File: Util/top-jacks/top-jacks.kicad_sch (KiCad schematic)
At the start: 6 parts, among them J1 Screw_Terminal_01x02, J4 Barrel_Jack_Switch, J5 Screw_Terminal_01x06, J6 Screw_Terminal_01x02

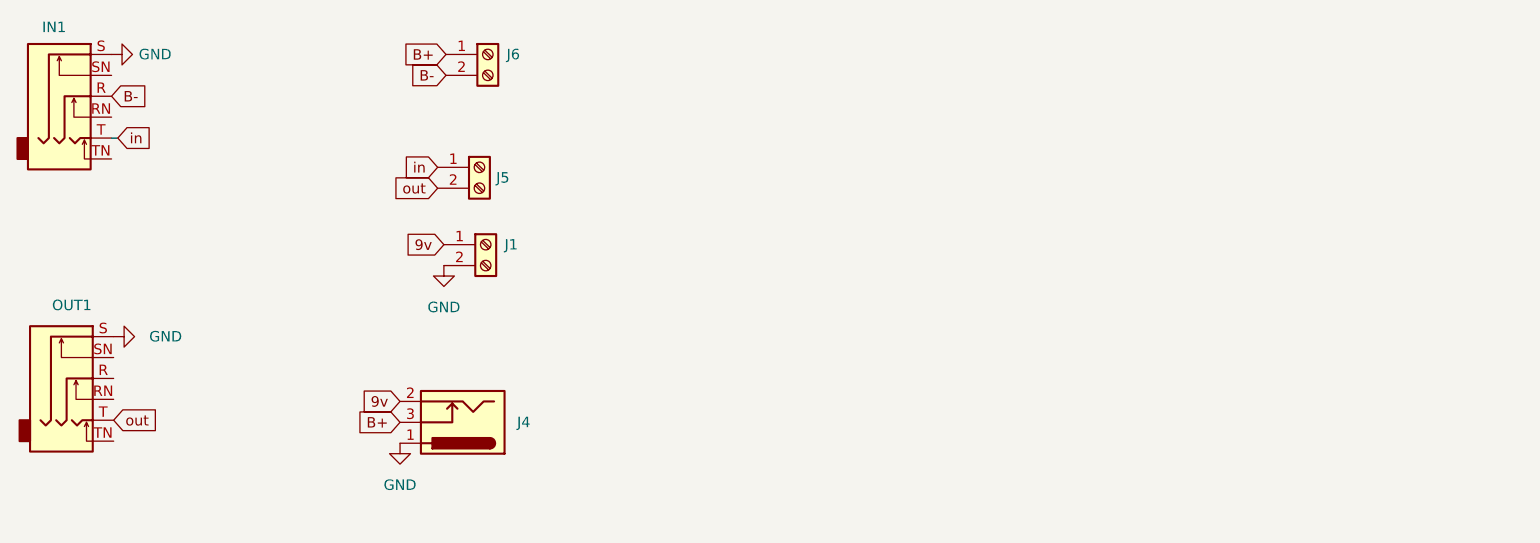
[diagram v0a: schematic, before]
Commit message: replaced whiefuzz, and modified ejfuzzface
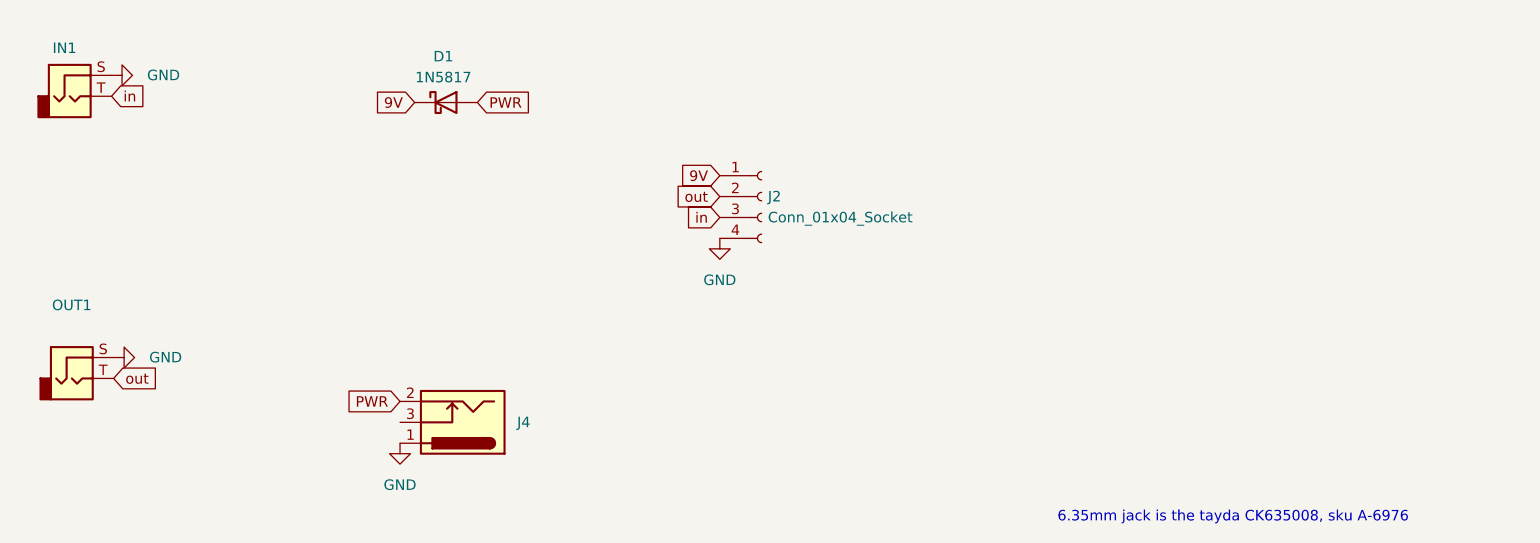
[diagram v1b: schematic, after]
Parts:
- removed J1, J6: Screw_Terminal_01x02, Connector_PinHeader_2.54mm:PinHeader_1x02_P2.54mm_Vertical, symbol Connector:Screw_Terminal_01x02
- removed J5: Screw_Terminal_01x06, Connector_PinHeader_2.54mm:PinHeader_1x02_P2.54mm_Vertical, symbol Connector:Screw_Terminal_01x02
- added D1: 1N5817, Diode_THT:D_DO-41_SOD81_P10.16mm_Horizontal, symbol Diode:1N5817
- added J2: Conn_01x04_Socket, Connector_PinHeader_2.54mm:PinHeader_1x04_P2.54mm_Vertical, symbol Connector:Conn_01x04_Socket
- IN1, OUT1: footprint Connector_Audio:Jack_6.35mm_Neutrik_NMJ6HCD2_Horizontal -> pedals:6.35mm-audio-jack; symbol Connector_Audio:AudioJack3_Switch -> Connector_Audio:AudioJack2
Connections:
- net GND: now also J2.4 (Pin_4)
- net in: now also J2.3 (Pin_3)
- net out: now also J2.2 (Pin_2)
- net 9v renamed PWR
- net PWR: now also D1.2 (A)
- net B+: no longer names the net of J4.3
- removed net B-: IN1.R
- new net 9V: D1.1 (K), J2.1 (Pin_1)
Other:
- note added: "6.35mm jack is the tayda CK635008, sku A-6976"
